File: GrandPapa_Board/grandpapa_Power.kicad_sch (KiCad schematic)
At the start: 55 parts, among them J9 3.7V LiPo Single Cell, U1 FPF2701MX, U2 TPS61023DRLT, U3 INA180A4QDBVRQ1, U4 LT1576IS8-5#TRPBF, U5 FPF2124, U6 MCP73871, U9 INA180A4QDBVRQ1

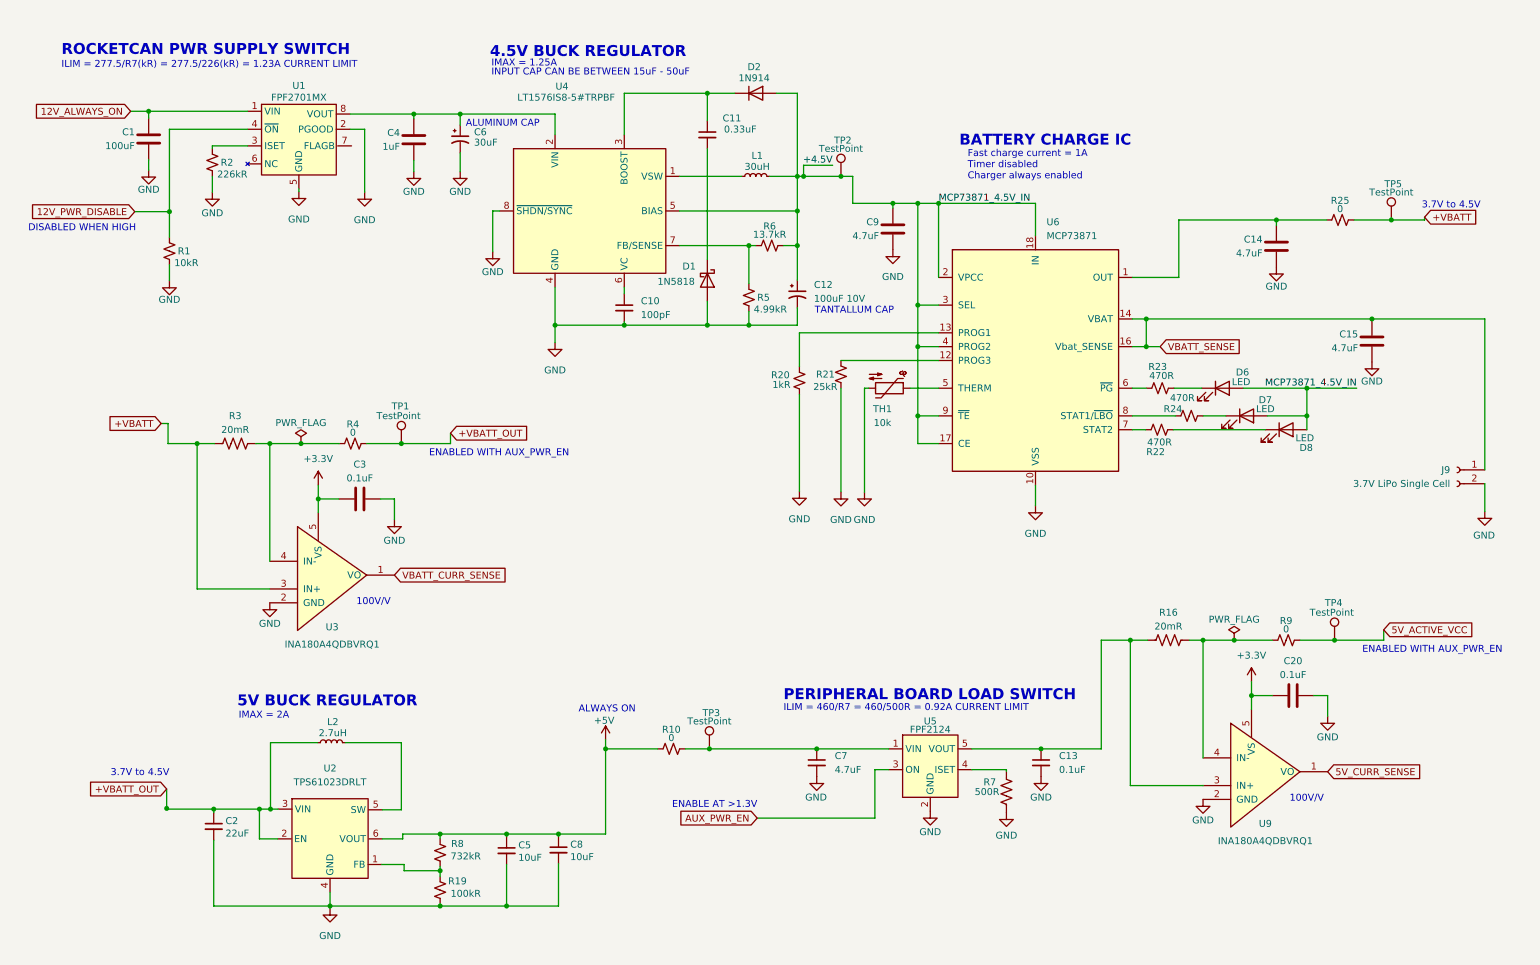
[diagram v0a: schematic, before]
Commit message: clean up schematic, fix some ERC errors
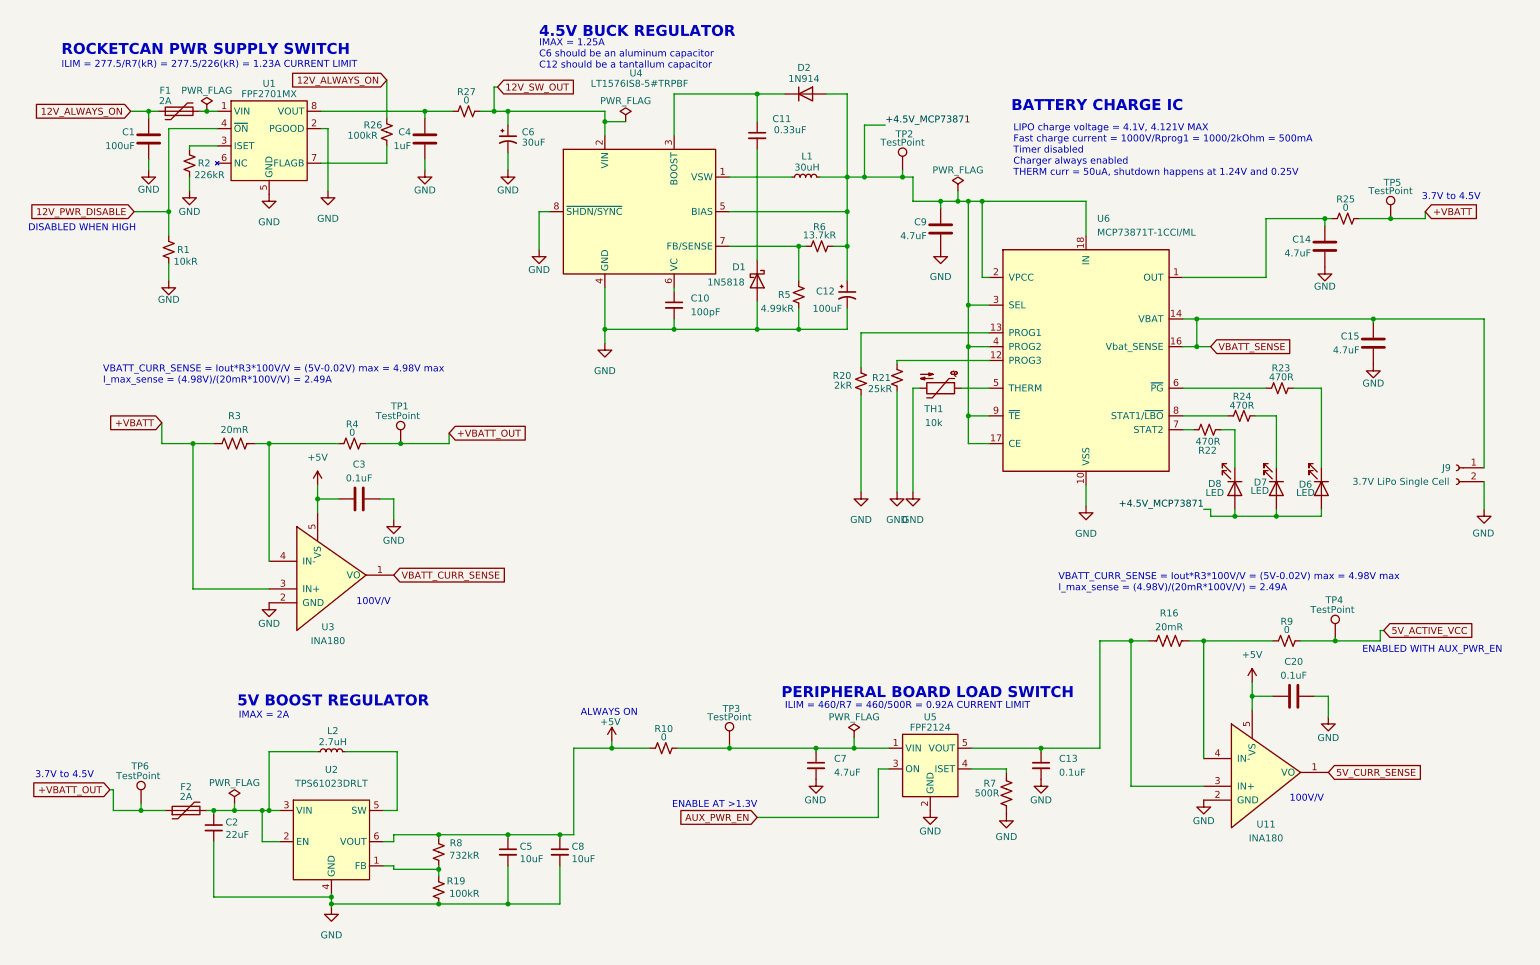
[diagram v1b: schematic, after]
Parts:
- removed U3, U9: INA180A4QDBVRQ1, Package_TO_SOT_SMD:SOT-23-5_HandSoldering, symbol payload2020_custom:INA180
- added F1, F2: 2A, symbol Device:Polyfuse
- added R26: 100kR, symbol Device:R_Small_US
- added R27: 0, symbol Device:R_Small_US
- added TP6: TestPoint, Connector_PinHeader_2.54mm:PinHeader_1x01_P2.54mm_Vertical, symbol Connector:TestPoint
- added U11, U3: INA180, symbol CANHW:INA180
- C12: value 100uF 10V -> 100uF
- R20: value 1kR -> 2kR
- U6: value MCP73871 -> MCP73871T-1CCI/ML
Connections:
- net +3V3 is gone; now on net +5V: C20.2, C3.2
- net +5V: now also U11.5 (VS), U3.5 (VS)
- net +VBATT: now also U3.3 (IN+)
- net +VBATT_OUT: now also F2.1, TP6.1; no longer C2.1, L2.1, U2.2 (EN), U2.3 (VIN)
- net 12V_ALWAYS_ON: now also F1.1, R26.2; no longer U1.1 (VIN)
- net 5V_CURR_SENSE: now also U11.1 (VO)
- net GND: now also U11.2 (GND), U3.2 (GND)
- net VBATT_CURR_SENSE: now also U3.1 (VO)
- net at C13.1, R16.2, U5.5 (VOUT): now also U11.3 (IN+)
- net at R3.1, R4.1: now also U3.4 (IN-)
- net at R16.1, R9.1: now also U11.4 (IN-)
- net at C4.1, U1.8 (VOUT): now also R27.1; no longer C6.1, U4.2 (VIN)
- net at U1.7 (FLAGB): now also R26.1
- net +4.5V renamed +4.5V_MCP73871
- new net: C2.1, F2.2, L2.1, U2.2 (EN), U2.3 (VIN)
- new net: F1.2, U1.1 (VIN)
- new net 12V_SW_OUT: C6.1, R27.2, U4.2 (VIN)
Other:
- note added: "5V BOOST REGULATOR"
- note added: "IMAX = 1.25A C6 should be an aluminum capacitor C12 should be a tantallum capacitor"
- note added: "LIPO charge voltage = 4.1V, 4.121V MAX Fast charge current = 1000V/Rprog1 = 1000/2kOhm = 500mA Timer disabled Charger always enabled THERM curr = 50uA, shutdown happens at 1.24V and 0.25V"
- note added: "VBATT_CURR_SENSE = Iout*R3*100V/V = (5V-0.02V) max = 4.98V max I_max_sense = (4.98V)/(20mR*100V/V) = 2.49A"
- note removed: "5V BUCK REGULATOR"
- note removed: "ALUMINUM CAP"
- note removed: "Fast charge current = 1A Timer disabled Charger always enabled"
- note removed: "IMAX = 1.25A"
- note removed: "INPUT CAP CAN BE BETWEEN 15uF - 50uF"
- note removed: "TANTALLUM CAP"
- moved on the sheet: C10, C11, C12, C13, C14, C4, C6, C7, C9, D1, D2, D6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

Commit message: move 12V shutoff to reg, rm motor stuff, subsheet/global pin redesign
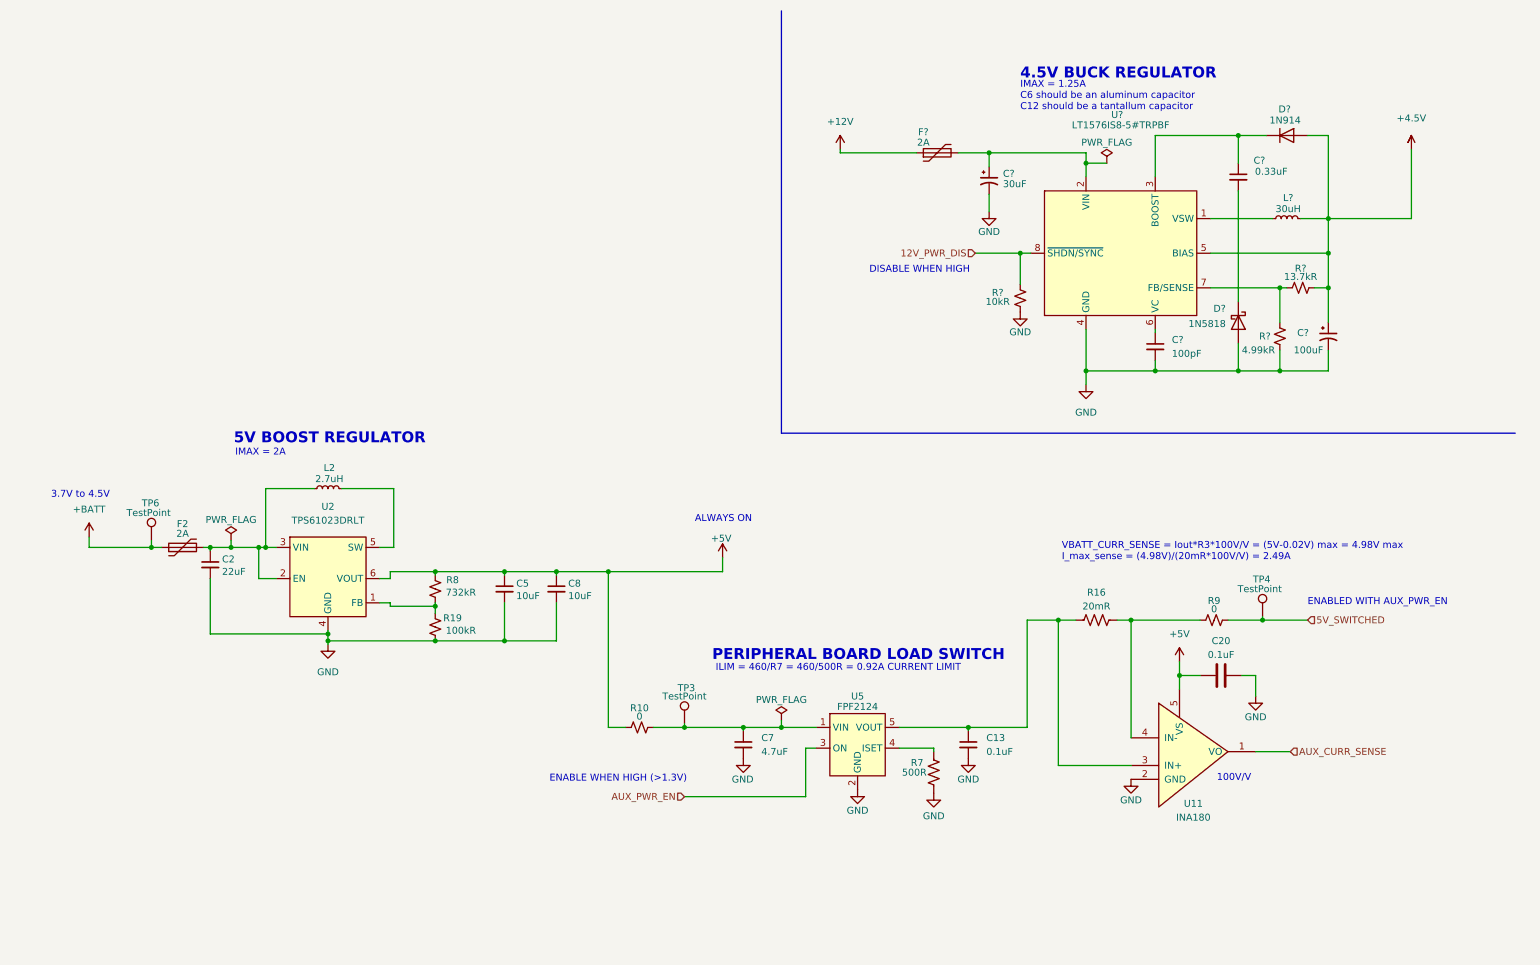
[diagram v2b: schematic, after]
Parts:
- removed C1: 100uF, symbol Device:C
- removed C10: 100pF, symbol Device:C_Small
- removed C11: 0.33uF, symbol Device:C_Small
- removed C12: 100uF, symbol Device:C_Polarized_Small_US
- removed C14, C15, C9: 4.7uF, symbol Device:C
- removed C3: 0.1uF, Capacitor_SMD:C_0805_2012Metric_Pad1.18x1.45mm_HandSolder, symbol Device:C
- removed C4: 1uF, symbol Device:C
- removed C6: 30uF, symbol Device:C_Polarized_Small_US
- removed D1: 1N5818, Diode_THT:D_DO-41_SOD81_P10.16mm_Horizontal, symbol Diode:1N5818
- removed D2: 1N914, Diode_THT:D_DO-35_SOD27_P7.62mm_Horizontal, symbol Diode:1N914
- removed D6, D7, D8: LED, symbol Device:LED
- removed F1: 2A, symbol Device:Polyfuse
- removed J9: 3.7V LiPo Single Cell, Connector_JST:JST_PH_S2B-PH-K_1x02_P2.00mm_Horizontal, symbol Connector:Conn_01x02_Female
- removed L1: 30uH, symbol Device:L_Small
- removed R1: 10kR, symbol Device:R_Small_US
- removed R2: 226kR, symbol Device:R_Small_US
- removed R20: 2kR, symbol Device:R_Small_US
- removed R21: 25kR, symbol Device:R_Small_US
- removed R22, R23, R24: 470R, symbol Device:R_Small_US
- removed R25, R27, R4: 0, symbol Device:R_Small_US
- removed R26: 100kR, symbol Device:R_Small_US
- removed R3: 20mR, Resistor_SMD:R_1206_3216Metric_Pad1.30x1.75mm_HandSolder, symbol Device:R_US
- removed R5: 4.99kR, symbol Device:R_Small_US
- removed R6: 13.7kR, symbol Device:R_Small_US
- removed TH1: 10k, symbol Device:Thermistor_NTC
- removed TP1: TestPoint, Connector_PinHeader_2.54mm:PinHeader_1x01_P2.54mm_Vertical, symbol Connector:TestPoint
- removed TP2, TP5: TestPoint, symbol Connector:TestPoint
- removed U1: FPF2701MX, symbol grandpapa board:FPF2701MX
- removed U3: INA180, symbol CANHW:INA180
- removed U4: LT1576IS8-5#TRPBF, symbol grandpapa board:LT1576IS8-5#TRPBF
- removed U6: MCP73871T-1CCI/ML, Package_DFN_QFN:QFN-20-1EP_4x4mm_P0.5mm_EP2.5x2.5mm, symbol Battery_Management:MCP73871
- added C?: 100pF, symbol Device:C_Small
- added C?: 0.33uF, symbol Device:C_Small
- added C?: 100uF, symbol Device:C_Polarized_Small_US
- added C?: 30uF, symbol Device:C_Polarized_Small_US
- added D?: 1N914, Diode_THT:D_DO-35_SOD27_P7.62mm_Horizontal, symbol Diode:1N914
- added D?: 1N5818, Diode_THT:D_DO-41_SOD81_P10.16mm_Horizontal, symbol Diode:1N5818
- added F?: 2A, symbol Device:Polyfuse
- added L?: 30uH, symbol Device:L_Small
- added R?: 4.99kR, symbol Device:R_Small_US
- added R?: 10kR, symbol Device:R_Small_US
- added R?: 13.7kR, symbol Device:R_Small_US
- added U?: LT1576IS8-5#TRPBF, symbol grandpapa board:LT1576IS8-5#TRPBF
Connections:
- net GND: now also C?.2, C?.2, C?.2, D?.2 (A), R?.1, R?.2, U?.4 (GND)
- net +VBATT_OUT renamed +BATT
- net 5V_ACTIVE_VCC renamed 5V_SWITCHED
- net 5V_CURR_SENSE renamed AUX_CURR_SENSE
- new net: C?.1, D?.1 (K), U?.3 (BOOST)
- new net: L?.1, U?.1 (VSW)
- new net: C?.1, F?.2, U?.2 (VIN)
- new net: C?.1, U?.6 (VC)
- new net: R?.1, R?.2, U?.7 (FB/SENSE)
- new net: C?.2, D?.1 (K)
- new net +12V: F?.1
- new net +4.5V: C?.1, D?.2 (A), L?.2, R?.2, U?.5 (BIAS)
- new net 12V_PWR_DIS: R?.1, U?.8 (~{SHDN/SYNC})
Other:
- note added: "DISABLE WHEN HIGH"
- note added: "ENABLE WHEN HIGH (>1.3V)"
- note removed: "BATTERY CHARGE IC"
- note removed: "DISABLED WHEN HIGH"
- note removed: "ENABLE AT >1.3V"
- note removed: "ILIM = 277.5/R7(kR) = 277.5/226(kR) = 1.23A CURRENT LIMIT"
- note removed: "LIPO charge voltage = 4.1V, 4.121V MAX Fast charge current = 1000V/Rprog1 = 1000/2kOhm = 500mA Timer disabled Charger always enabled THERM curr = 50uA, shutdown happens at 1.24V and 0.25V"
- note removed: "ROCKETCAN PWR SUPPLY SWITCH"
- moved on the sheet: C13, C2, C20, C5, C7, C8, F2, L2, R10, R16, R19, R7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

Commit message: fix erc
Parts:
- gave numbers to parts that had none: 12
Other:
- moved on the sheet: TP6
